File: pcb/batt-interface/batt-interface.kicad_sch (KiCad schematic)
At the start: 10 parts, among them IC1 MCP73831T-2ACI_OT, J1 UJC-H-G-SMT-2-P6-TR, J2 Battery, J3 Load

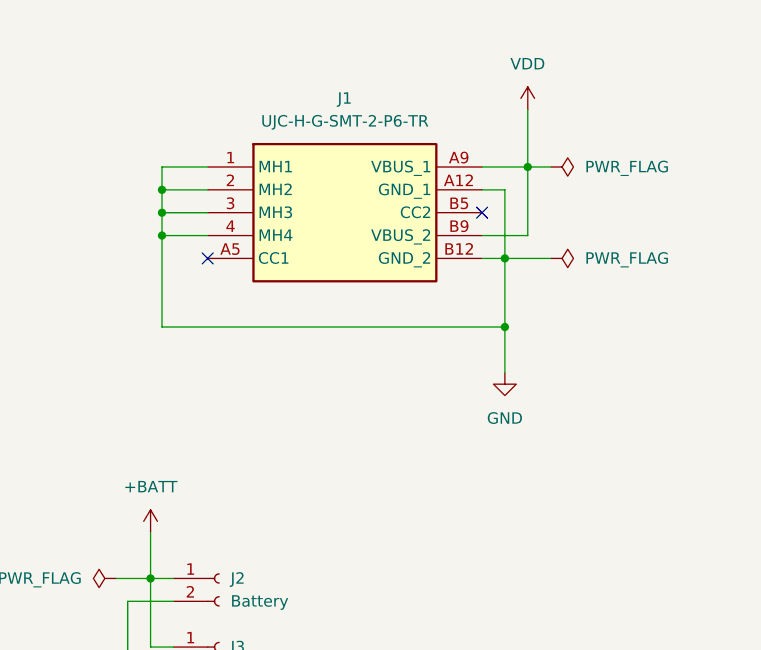
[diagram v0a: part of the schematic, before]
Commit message: Added pull down resistors for CC1 and CC2 to ensure proper charging.
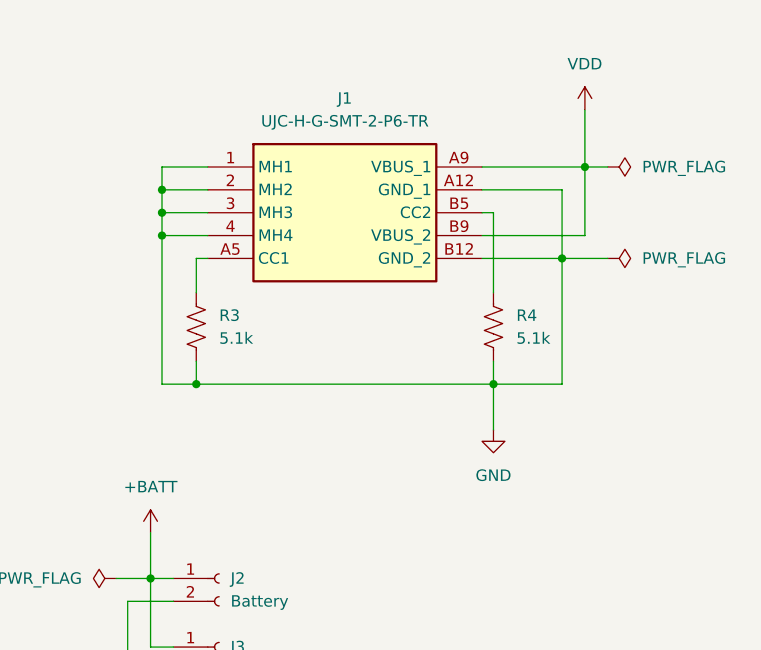
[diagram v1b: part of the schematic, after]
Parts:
- added R3, R4: 5.1k, Resistor_SMD:R_0805_2012Metric_Pad1.20x1.40mm_HandSolder, symbol Device:R_US
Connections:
- net GND: now also R3.2, R4.2
- net at J1.A5 (CC1): now also R3.1
- net at J1.B5 (CC2): now also R4.1
- no-connect marks 2 -> 0
